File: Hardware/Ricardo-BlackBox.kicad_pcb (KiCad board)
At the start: 4 copper layers, 45.1 x 35.1 mm, 83 parts, among them J1 RBUS, J2 USB_C_Receptacle_USB2.0, J3 Conn_01x08_Pin, U1 ESP32-S3, U2 SN65HVD230, U3 LM66200DRLR, U4 MAX77827AEFD+T, U5 SC4215ASTRT, U7 LM66200DRLR, Y1 R940000171

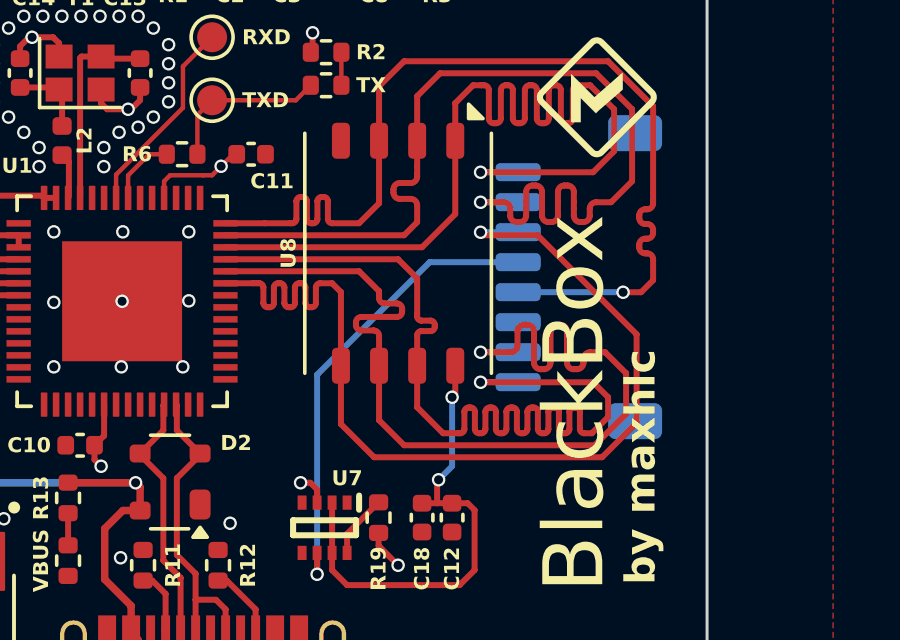
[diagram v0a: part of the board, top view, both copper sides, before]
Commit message: Update length matching
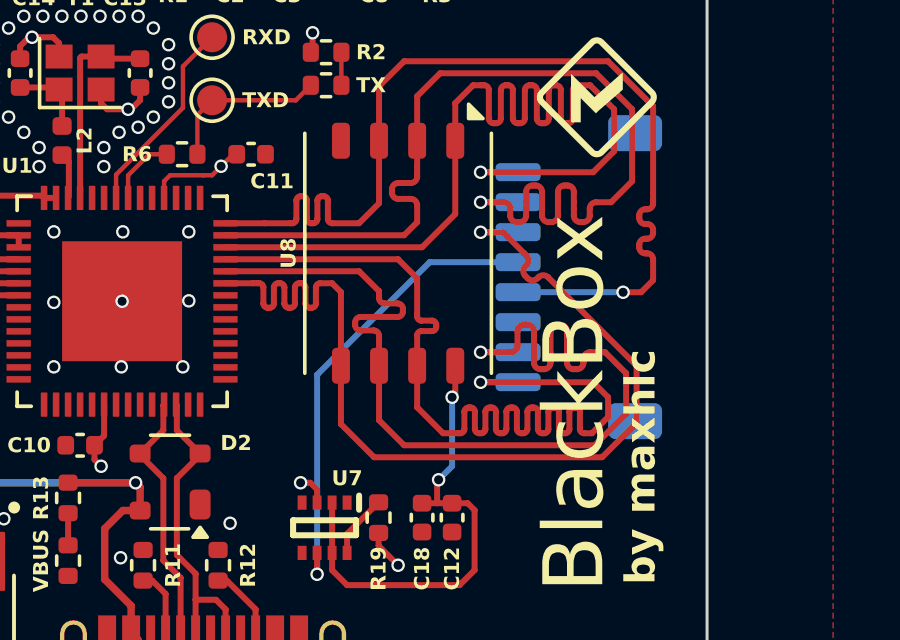
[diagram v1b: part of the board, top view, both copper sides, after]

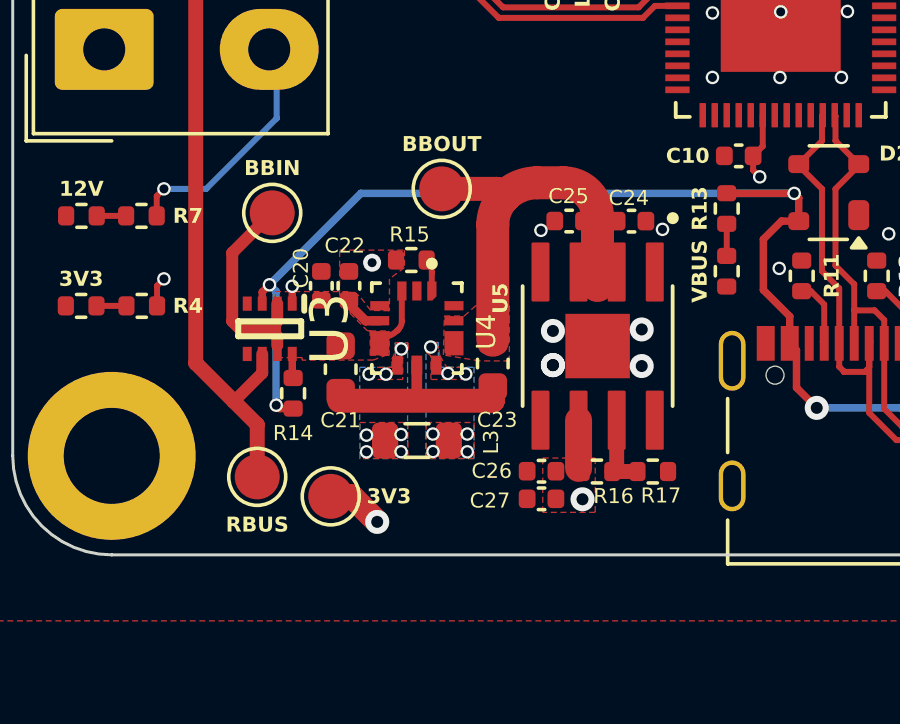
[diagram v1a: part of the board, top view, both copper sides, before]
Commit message: Updated buckboost silkscreen labels
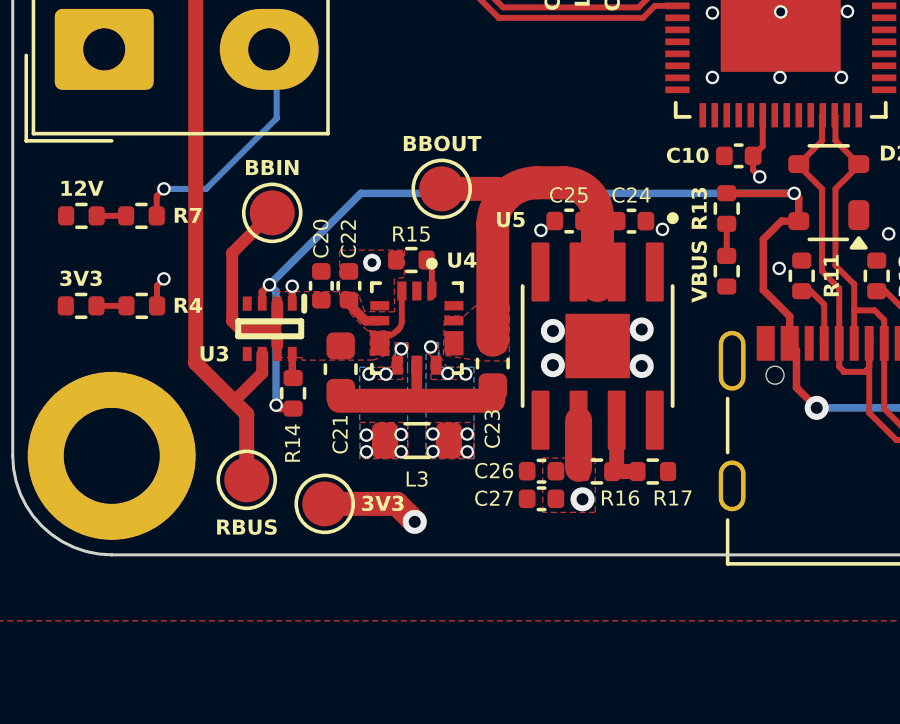
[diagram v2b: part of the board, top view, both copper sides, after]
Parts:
- moved RBUS 0.36 mm to (86.9, 78.4)
- moved 3V3 0.32 mm to (89.5, 79.2)
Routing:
- net +3V3: track 24.3 -> 25.6 mm
- net GND: vias 53 -> 52

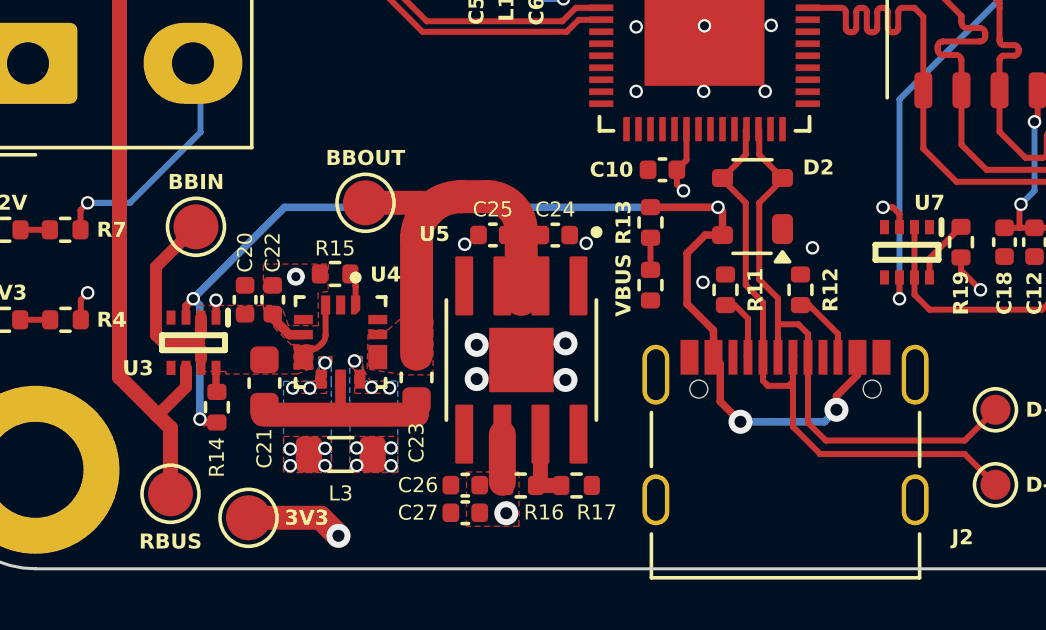
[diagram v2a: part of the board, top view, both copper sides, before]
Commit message: Increased VBUS trace widths and rerouted
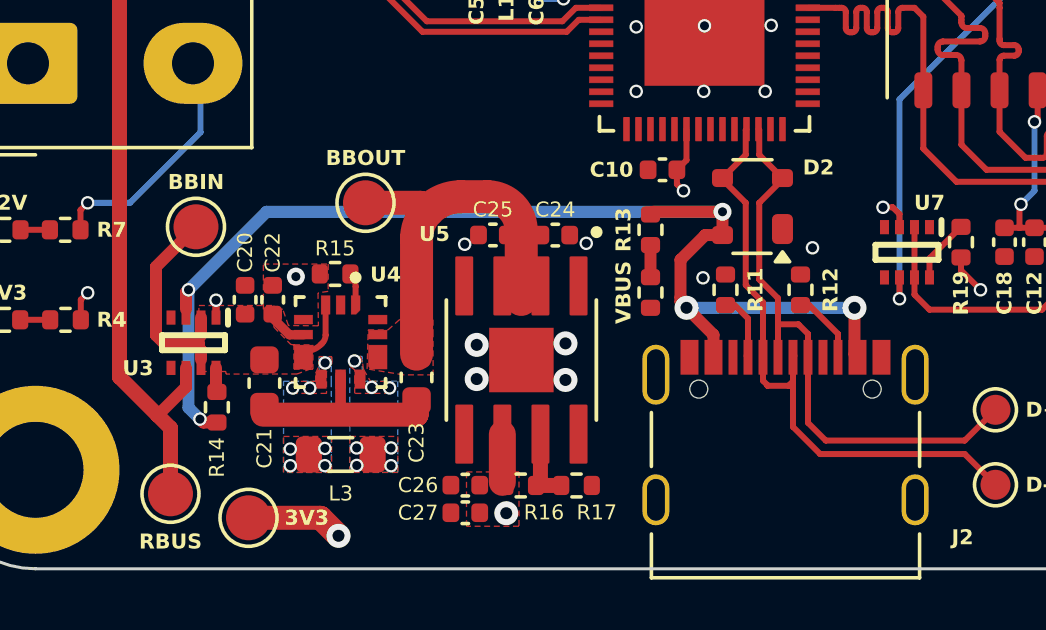
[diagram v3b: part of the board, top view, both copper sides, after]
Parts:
- moved R13 0.25 mm to (102.9, 69.6)
- moved VBUS 0.25 mm to (102.9, 71.7)

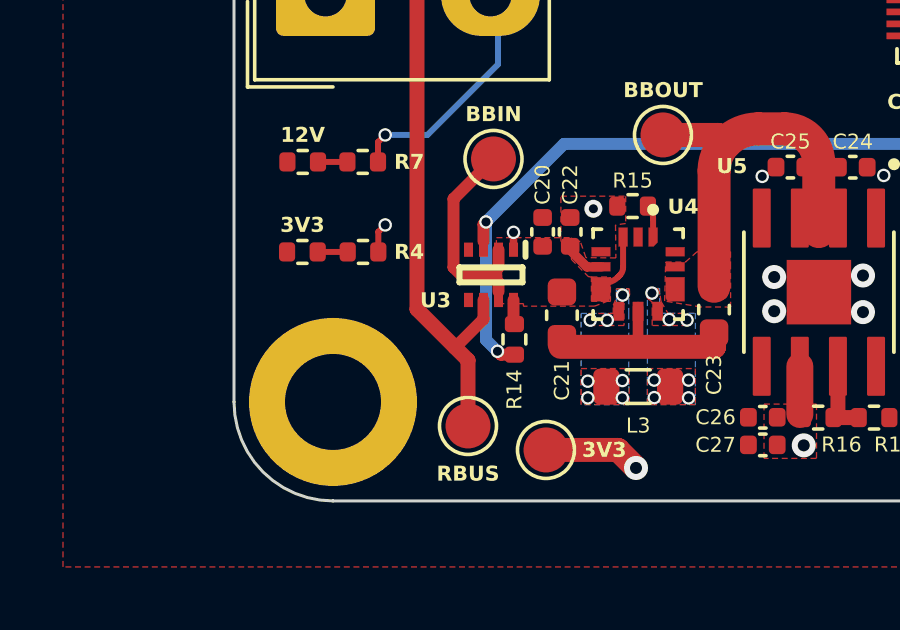
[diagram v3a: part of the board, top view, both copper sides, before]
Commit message: Updated RBUS trace
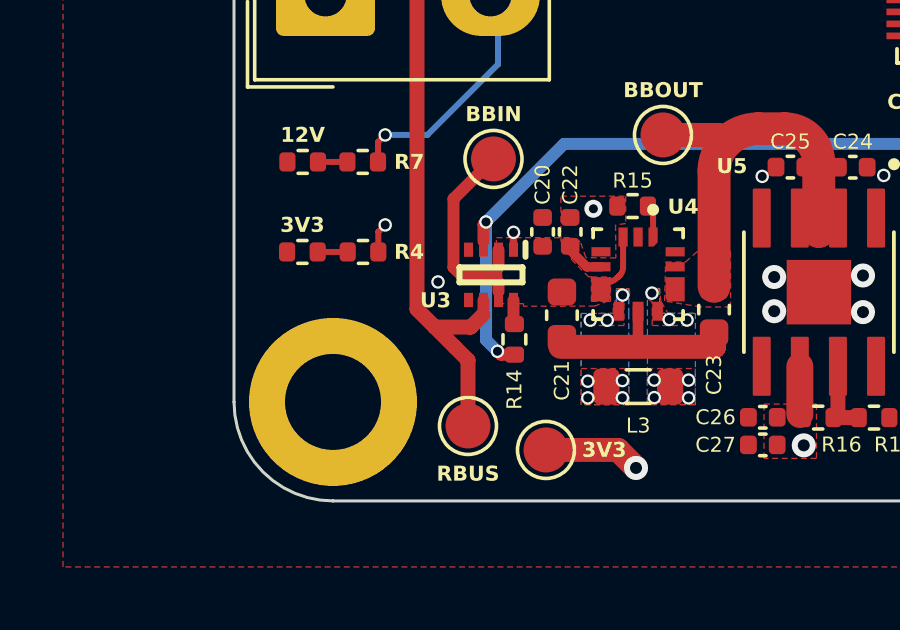
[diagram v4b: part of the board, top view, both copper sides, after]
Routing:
- net GND: vias 52 -> 53
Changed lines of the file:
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@@
 	)
 	(via
+		(at 85.925 73.59)
+		(size 0.45)
+		(drill 0.3)
+		(layers "F.Cu" "B.Cu")
+		(free yes)
+		(net 1)
+	)
+	(via
 		(at 103.354 53.29)
 		(size 0.45)
@@
 	)
 	(segment
+		(start 87.441888 74.191882)
+		(end 87.441888 74.673112)
+		(width 0.4)
+		(layer "F.Cu")
+		(net 4)
+	)
+	(segment
+		(start 86.977048 75.094222)
+		(end 87.020778 75.094222)
+		(width 0.5)
+		(layer "F.Cu")
+		(net 4)
+	)
+	(segment
 		(start 86.925 76.198444)
 		(end 86.925 78.39)
@@
 	)
 	(segment
-		(start 87.441888 74.829382)
-		(end 87.441888 74.191882)
+		(start 87.441888 74.673112)
+		(end 87.425 74.69)
 		(width 0.4)
 		(layer "F.Cu")
@@
 	)
 	(segment
-		(start 86.502048 75.769222)
-		(end 87.441888 74.829382)
-		(width 0.4)
+		(start 86.495778 75.769222)
+		(end 85.820778 75.094222)
+		(width 0.5)
 		(layer "F.Cu")
 		(net 4)
@@
 	)
 	(segment
-		(start 86.495778 75.769222)
-		(end 85.225 74.498444)
+		(start 87.020778 75.094222)
+		(end 87.425 74.69)
 		(width 0.5)
 		(layer "F.Cu")
@@
 	)
 	(segment
-		(start 86.495778 75.769222)
-		(end 86.502048 75.769222)
-		(width 0.4)
+		(start 85.820778 75.094222)
+		(end 85.225 74.498444)
+		(width 0.5)
+		(layer "F.Cu")
+		(net 4)
+	)
+	(segment
+		(start 86.977048 75.094222)
+		(end 85.820778 75.094222)
+		(width 0.5)
 		(layer "F.Cu")
 		(net 4)
@@
 	)
 	(zone
+		(net 1)
+		(net_name "GND")
+		(layer "F.Cu")
+		(name "$teardrop_padvia$")
+		(hatch full 0.1)
+		(priority 30002)
+		(attr
+			(teardrop
+				(type padvia)
+			)
+		)
+		(connect_pads yes
+			(clearance 0)
+		)
+		(min_thickness 0.0254)
+		(filled_areas_thickness no)
+		(fill yes
+			(thermal_gap 0.5)
+			(thermal_bridge_width 0.5)
+			(island_removal_mode 1)
+			(island_area_min 10)
+		)
+		(polygon
+			(pts
+				(xy 88.316888 72.386882) (xy 88.566888 72.386882) (xy 88.649761 72.022986) (xy 88.441888 71.935882)
+				(xy 88.234015 72.022986)
+			)
+		)
+	)
+	(zone
 		(net 7)
 		(net_name "/Power/BBOUT")
@@
 	)
 	(zone
-		(net 3)
-		(net_name "VBUS")
-		(layer "F.Cu")
-		(name "$teardrop_padvia$")
-		(hatch full 0.1)
-		(priority 30001)
-		(attr
-			(teardrop
-				(type padvia)
-			)
-		)
-		(connect_pads yes
-			(clearance 0)
-		)
-		(min_thickness 0.0254)
-		(filled_areas_thickness no)
-		(fill yes
-			(thermal_gap 0.5)
-			(thermal_bridge_width 0.5)
-			(island_removal_mode 1)
-			(island_area_min 10)
-		)
-		(polygon
-			(pts
-				(xy 87.241888 72.023468) (xy 87.641888 72.023468) (xy 87.732873 71.676104) (xy 87.525 71.589) (xy 87.3 71.59)
-			)
-		)
-	)
-	(zone
 		(net 0)
 		(net_name "")
@@
 	)
 	(zone
+		(net 3)
+		(net_name "VBUS")
+		(layer "F.Cu")
+		(name "$teardrop_padvia$")
+		(hatch full 0.1)
+		(priority 30001)
+		(attr
+			(teardrop
+				(type padvia)
+			)
+		)
+		(connect_pads yes
+			(clearance 0)
+		)
+		(min_thickness 0.0254)
+		(filled_areas_thickness no)
+		(fill yes
+			(thermal_gap 0.5)
+			(thermal_bridge_width 0.5)
+			(island_removal_mode 1)
+			(island_area_min 10)
+		)
+		(polygon
+			(pts
+				(xy 87.241888 72.023468) (xy 87.641888 72.023468) (xy 87.732873 71.676104) (xy 87.525 71.589) (xy 87.3 71.59)
+			)
+		)
+	)
+	(zone
 		(net 2)
 		(net_name "+3V3")
@@
 		(net 1)
 		(net_name "GND")
-		(layer "F.Cu")
-		(name "$teardrop_padvia$")
-		(hatch full 0.1)
-		(priority 30002)
-		(attr
-			(teardrop
-				(type padvia)
-			)
-		)
+		(layer "In1.Cu")
+		(hatch edge 0.5)
+		(priority 1)
 		(connect_pads yes
 			(clearance 0)
 		)
-		(min_thickness 0.0254)
+		(min_thickness 0.25)
 		(filled_areas_thickness no)
 		(fill yes
 			(thermal_gap 0.5)
 			(thermal_bridge_width 0.5)
-			(island_removal_mode 1)
-			(island_area_min 10)
 		)
 		(polygon
 			(pts
-				(xy 88.316888 72.386882) (xy 88.566888 72.386882) (xy 88.649761 72.022986) (xy 88.441888 71.935882)
-				(xy 88.234015 72.022986)
+				(xy 70.925 85.59) (xy 70.925 40.59) (xy 130.925 40.59) (xy 130.925 85.59)
 			)
 		)
 	)
 	(zone
-		(net 1)
-		(net_name "GND")
-		(layer "In1.Cu")
+		(net 2)
+		(net_name "+3V3")
+		(layer "In2.Cu")
 		(hatch edge 0.5)
 		(priority 1)
@@
 		(polygon
 			(pts
-				(xy 70.925 85.59) (xy 70.925 40.59) (xy 130.925 40.59) (xy 130.925 85.59)
+				(xy 68.425 38.09) (xy 68.425 88.09) (xy 133.425 88.09) (xy 133.425 38.09)
 			)
 		)
 	)
 	(zone
-		(net 2)
-		(net_name "+3V3")
-		(layer "In2.Cu")
-		(hatch edge 0.5)
-		(priority 1)
+		(net 3)
+		(net_name "VBUS")
+		(layer "B.Cu")
+		(name "$teardrop_padvia$")
+		(hatch full 0.1)
+		(priority 30002)
+		(attr
+			(teardrop
+				(type padvia)
+			)
+		)
 		(connect_pads yes
 			(clearance 0)
 		)
-		(min_thickness 0.25)
+		(min_thickness 0.0254)
 		(filled_areas_thickness no)
 		(fill yes
 			(thermal_gap 0.5)
 			(thermal_bridge_width 0.5)
+			(island_removal_mode 1)
+			(island_area_min 10)
 		)
 		(polygon
 			(pts
-				(xy 68.425 38.09) (xy 68.425 88.09) (xy 133.425 88.09) (xy 133.425 38.09)
+				(xy 87.984619 71.413224) (xy 87.701776 71.130381) (xy 87.365901 71.430901) (xy 87.524293 71.590707)
+				(xy 87.684099 71.749099)
+			)
+		)
+	)
+	(zone
+		(net 3)
+		(net_name "VBUS")
+		(layer "B.Cu")
+		(name "$teardrop_padvia$")
+		(hatch full 0.1)
+		(priority 30001)
+		(attr
+			(teardrop
+				(type padvia)
+			)
+		)
+		(connect_pads yes
+			(clearance 0)
+		)
+		(min_thickness 0.0254)
+		(filled_areas_thickness no)
+		(fill yes
+			(thermal_gap 0.5)
+			(thermal_bridge_width 0.5)
+			(island_removal_mode 1)
+			(island_area_min 10)
+		)
+		(polygon
+			(pts
+				(xy 87.730112 75.442263) (xy 87.447269 75.725106) (xy 87.747789 76.060981) (xy 87.907595 75.902589)
+				(xy 88.065987 75.742783)
 			)
 		)
@@
 	)
 	(zone
-		(net 3)
-		(net_name "VBUS")
-		(layer "B.Cu")
-		(name "$teardrop_padvia$")
-		(hatch full 0.1)
-		(priority 30000)
-		(attr
-			(teardrop
-				(type padvia)
-			)
-		)
-		(connect_pads yes
-			(clearance 0)
-		)
-		(min_thickness 0.0254)
-		(filled_areas_thickness no)
-		(fill yes
-			(thermal_gap 0.5)
-			(thermal_bridge_width 0.5)
-			(island_removal_mode 1)
-			(island_area_min 10)
-		)
-		(polygon
-			(pts
-				(xy 87.325 72.04) (xy 87.725 72.04) (xy 87.75 71.59) (xy 87.525 71.589) (xy 87.3 71.59)
-			)
-		)
-	)
-	(zone
 		(net 1)
 		(net_name "GND")
@@
 		(name "$teardrop_padvia$")
 		(hatch full 0.1)
-		(priority 30002)
-		(attr
-			(teardrop
-				(type padvia)
-			)
-		)
-		(connect_pads yes
-			(clearance 0)
-		)
-		(min_thickness 0.0254)
-		(filled_areas_thickness no)
-		(fill yes
-			(thermal_gap 0.5)
-			(thermal_bridge_width 0.5)
-			(island_removal_mode 1)
-			(island_area_min 10)
-		)
-		(polygon
-			(pts
-				(xy 87.984619 71.413224) (xy 87.701776 71.130381) (xy 87.365901 71.430901) (xy 87.524293 71.590707)
-				(xy 87.684099 71.749099)
-			)
-		)
-	)
-	(zone
-		(net 3)
-		(net_name "VBUS")
-		(layer "B.Cu")
-		(name "$teardrop_padvia$")
-		(hatch full 0.1)
-		(priority 30001)
+		(priority 30000)
 		(attr
 			(teardrop
@@
 		(polygon
 			(pts
-				(xy 87.730112 75.442263) (xy 87.447269 75.725106) (xy 87.747789 76.060981) (xy 87.907595 75.902589)
-				(xy 88.065987 75.742783)
+				(xy 87.325 72.04) (xy 87.725 72.04) (xy 87.75 71.59) (xy 87.525 71.589) (xy 87.3 71.59)
 			)
 		)
